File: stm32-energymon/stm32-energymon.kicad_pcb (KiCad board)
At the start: 2 copper layers, 44.5 x 52.7 mm, 4 parts, among them J1 Conn_01x14, J2 Conn_01x02, J3 Conn_01x06, U1 blackpill

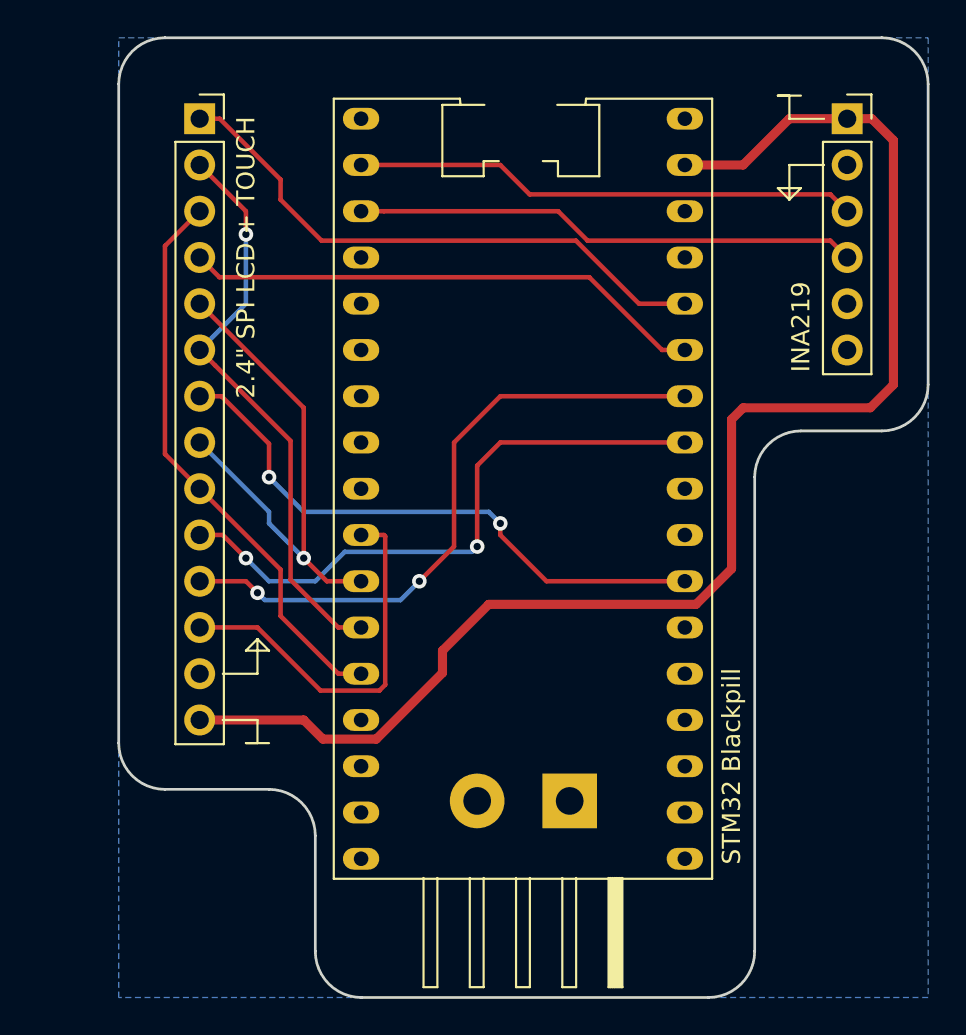
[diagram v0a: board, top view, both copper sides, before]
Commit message: Added 1.4" LCD to energymonitor
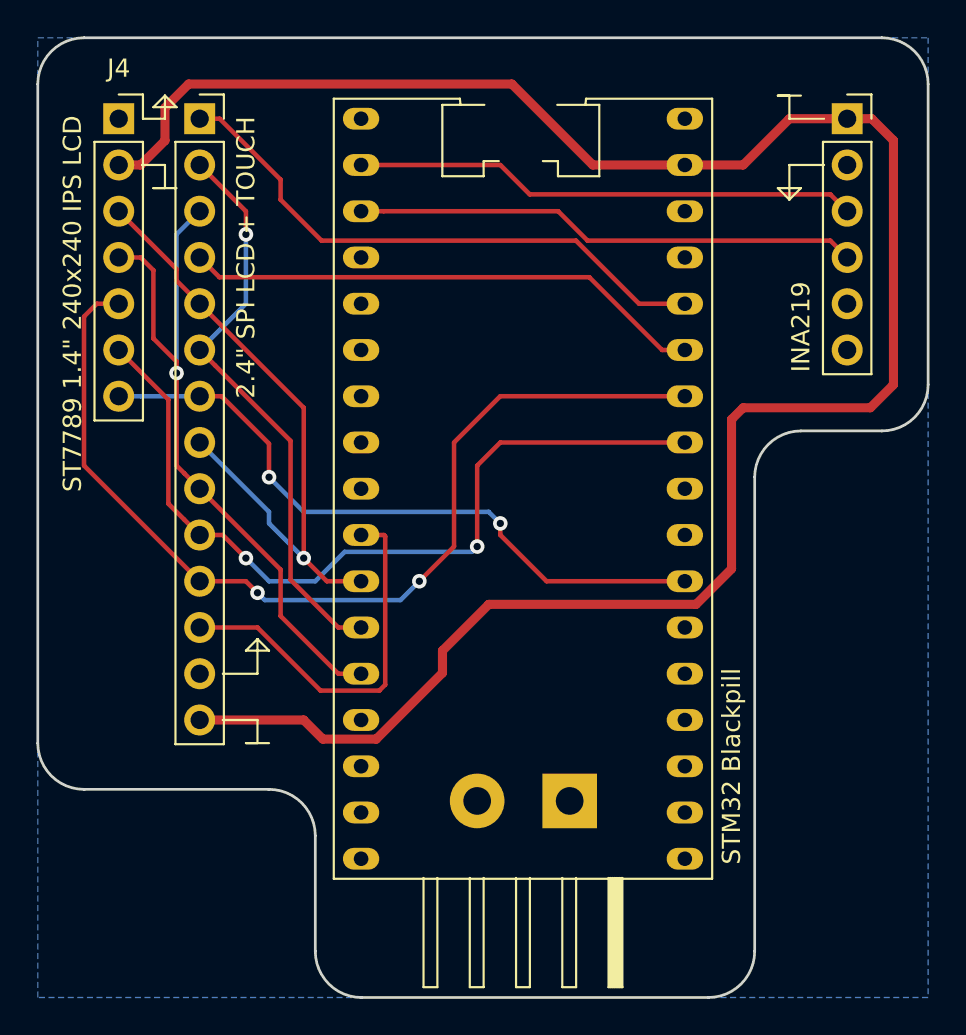
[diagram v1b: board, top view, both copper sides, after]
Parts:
- added J4: Conn_01x07, Connector_PinSocket_2.54mm:PinSocket_1x07_P2.54mm_Vertical, F.Cu at (83.8, 62.9)
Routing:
- net +3V3: track 78.5 -> 114.4 mm
- net /LCD_RST: track 35.1 -> 54.4 mm
- net /LCD_DC: track 33.5 -> 45.5 mm
- net /MOSI: track 31.4 -> 39.2 mm, vias 0 -> 1
- net /SCK: track 28.7 -> 35.7 mm
- net /LCD_BL: track 32.3 -> 36.7 mm
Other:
- board size 44.5 x 52.7 mm -> 48.9 x 52.7 mm
- board text added: "I2C SDA PB9 SCL PB8"
- board text added: "LCD"
- board text added: "MOSI PA7 MISO PA6 SCK PA5"
- board text added: "RST PB3 DC PA15 CS PA4 BL PA10"
- board text added: "SPI"
- board text added: "ST7789 1.4" 240x240 IPS LCD"
- board text added: "TS IRQ PB5 CS PB4"
